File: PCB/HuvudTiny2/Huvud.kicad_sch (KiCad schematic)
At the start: 117 parts, among them J1 Conn_02x02_Odd_Even, J12 USB_Micro-B_Molex-105017-0001, J2 DBG, J3 THERM, J4 FAN0, J5 FAN1, J6 Heater, J7 Endstop, J9 STEPPER, Q1 AO3400A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

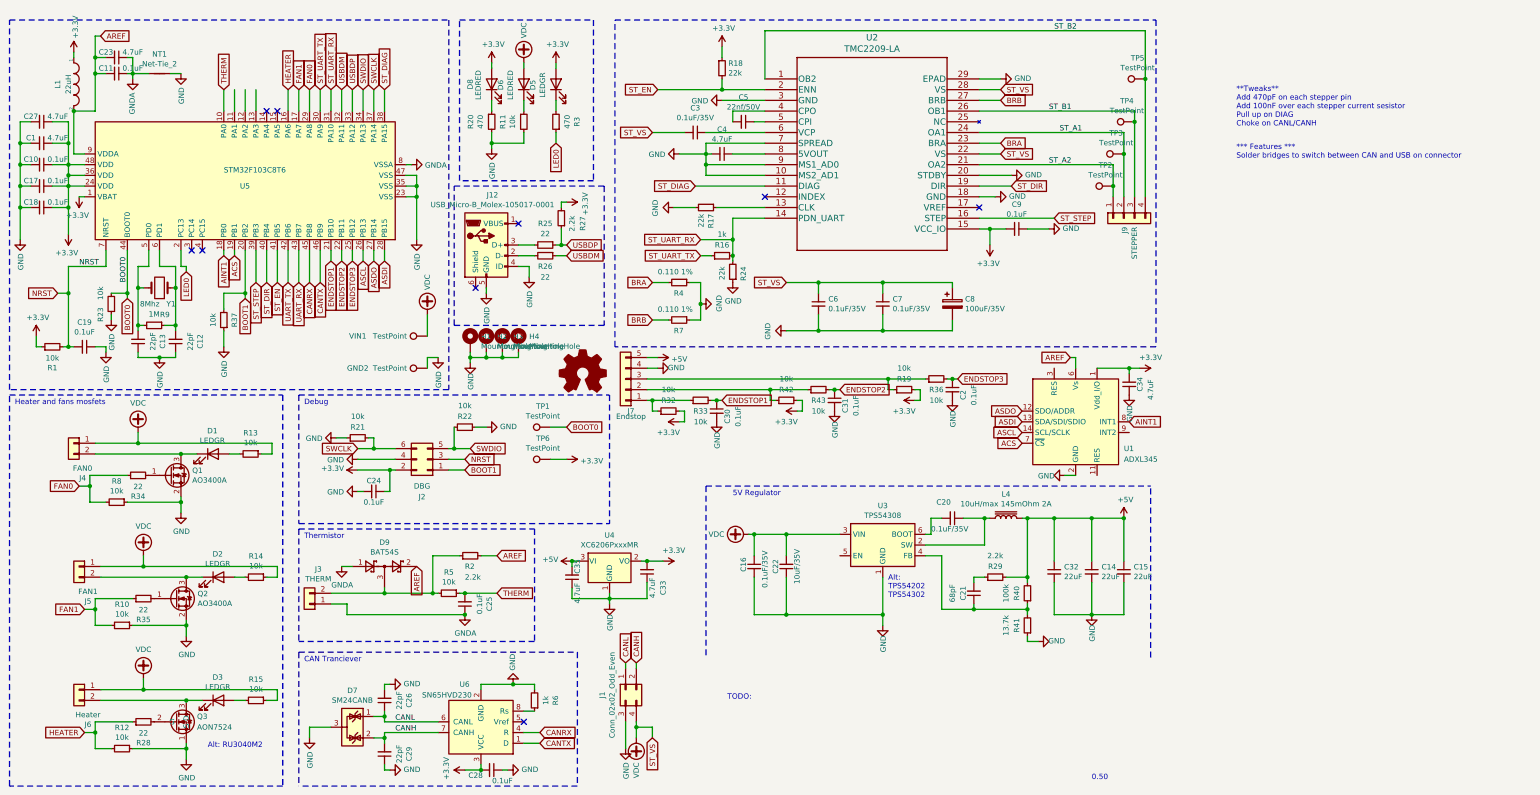
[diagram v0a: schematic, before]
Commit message: Power from USB, remove CAN. Update micro USB footprint. Update TMC footprint.
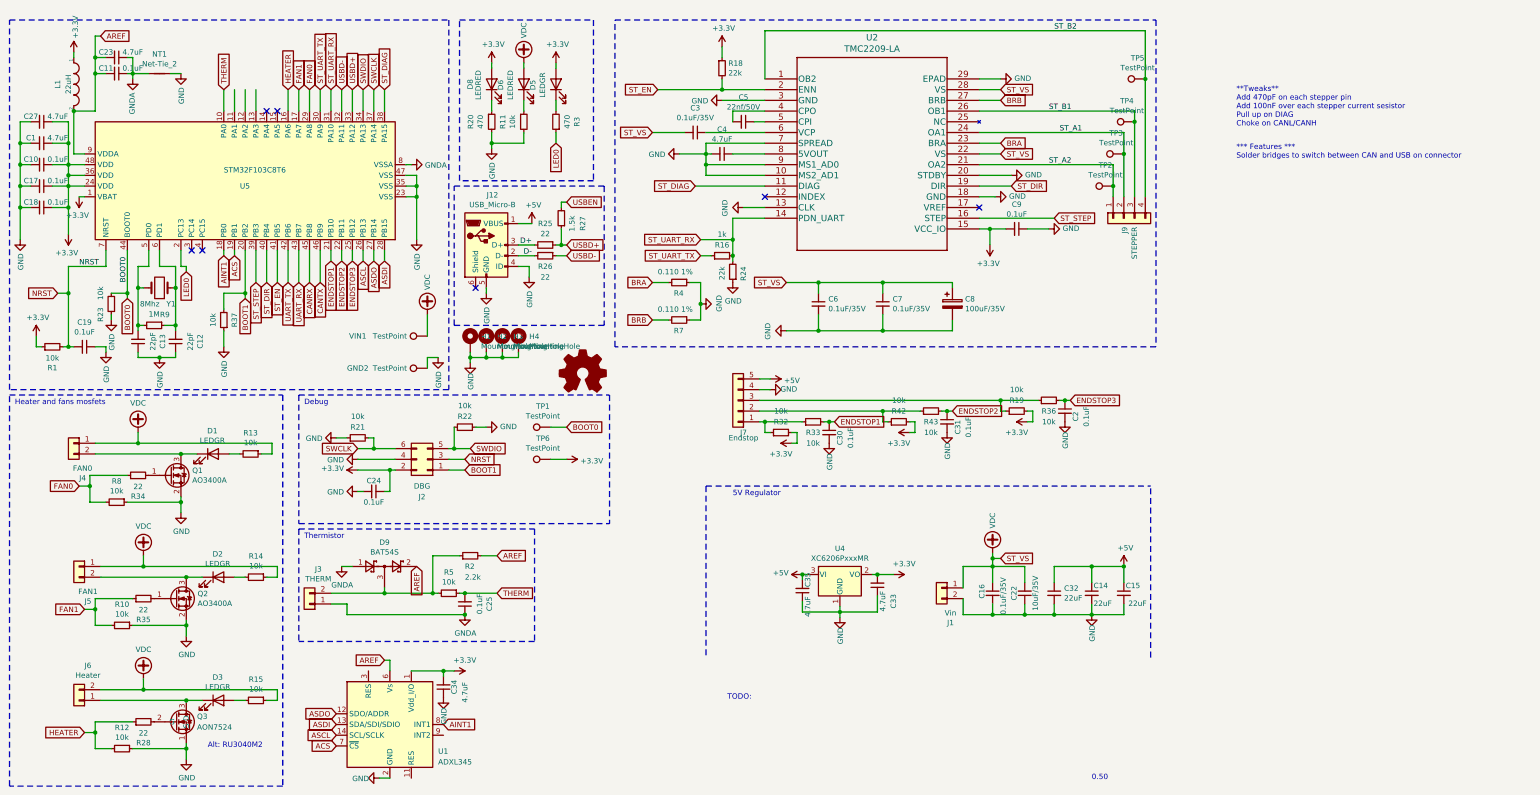
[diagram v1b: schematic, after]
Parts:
- removed C20: 0.1uF/35V, Capacitor_SMD:C_0603_1608Metric, symbol Device:C_Small
- removed C21: 68pF, Capacitor_SMD:C_0402_1005Metric, symbol Device:C_Small
- removed C26, C29: 22pF, Capacitor_SMD:C_0402_1005Metric, symbol Device:C_Small
- removed C28: 0.1uF, Capacitor_SMD:C_0402_1005Metric, symbol Device:C_Small
- removed D7: SM24CANB, Package_TO_SOT_SMD:SOT-23, symbol Power_Protection:NUP2105L
- removed J1: Conn_02x02_Odd_Even, Connector_Molex:Molex_Micro-Fit_3.0_43045-0400_2x02_P3.00mm_Horizontal, symbol Connector_Generic:Conn_02x02_Top_Bottom
- removed L4: 10uH/max 145mOhm 2A, Inductor_SMD:L_Sunlord_MWSA0518_5.4x5.2mm, symbol Device:L_Core_Iron
- removed R17: 22k, Resistor_SMD:R_0402_1005Metric, symbol Device:R_Small
- removed R29: 2.2k, Resistor_SMD:R_0402_1005Metric, symbol Device:R_Small
- removed R40: 100k, Resistor_SMD:R_0402_1005Metric, symbol Device:R_Small
- removed R41: 13.7k, Resistor_SMD:R_0402_1005Metric, symbol Device:R_Small
- removed R6: 1k, Resistor_SMD:R_0402_1005Metric, symbol Device:R_Small
- removed U3: TPS54308, Package_TO_SOT_SMD:SOT-23-6, symbol Regulator_Switching:TPS54308
- removed U6: SN65HVD230, Package_SO:SOIC-8_3.9x4.9mm_P1.27mm, symbol Interface_CAN_LIN:SN65HVD230
- added J1: Vin, Huvud:TerminalBlock_TE_282834-2_1x02_P2.54mm_Horizontal, symbol Connector_Generic:Conn_01x02
- J12: value USB_Micro-B_Molex-105017-0001 -> USB_Micro-B; footprint Connector_USB:USB_Micro-B_Molex-105017-0001 -> Huvud:MC-101C
- R27: value 2.2k -> 1.5k
- U2: footprint TMC2209:TMC2209-LA -> Huvud:TMC22xx_QFN
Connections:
- net +3V3: no longer R27.2
- net +5V: now also J12.1 (VBUS)
- net GND: now also U2.13 (CLK), J1.2 (Pin_2)
- net VDC: now also J6.2 (Pin_2), J1.1 (Pin_1); no longer J6.1 (Pin_1)
- net at D3.1 (K), Q3.3 (D): now also J6.1 (Pin_1); no longer J6.2 (Pin_2)
- net D-: now reaches J12.2 (D-), R26.2
- net D+: now reaches J12.3 (D+), R25.2
- net USBDM renamed USBD-
- net USBDP renamed USBD+
- new net USBEN: R27.2
- no-connect marks 9 -> 7
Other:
- note removed: "Alt: TPS54202 TPS54302"
- note removed: "CAN Tranciever"
- moved on the sheet: C14, C15, C16, C2, C22, C30, C31, C32, C33, C34, C35, J6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

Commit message: Improve power routing. Fix TH input protection.
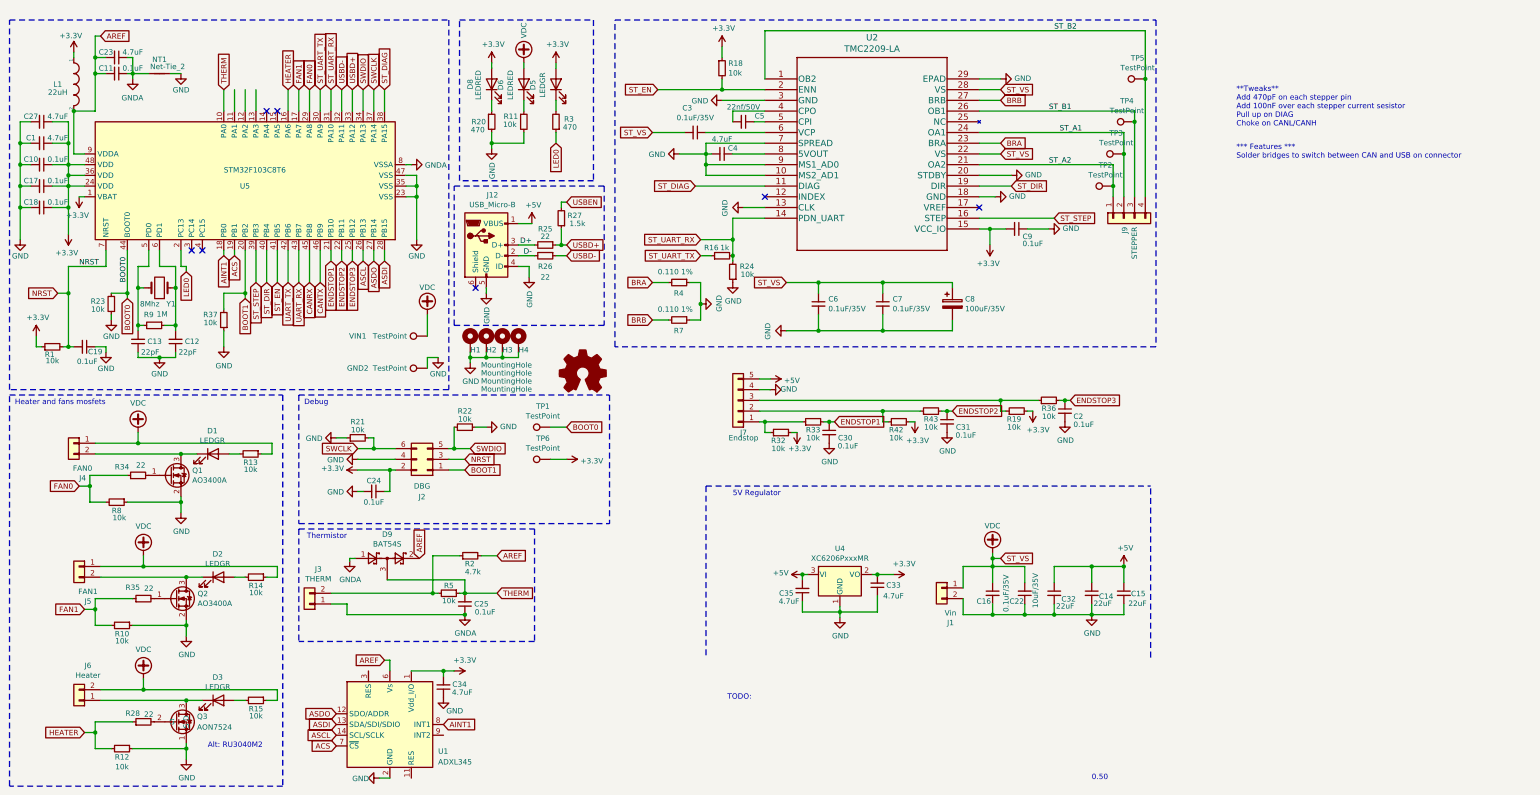
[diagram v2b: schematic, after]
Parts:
- R18, R24: value 22k -> 10k
- R2: value 2.2k -> 4.7k
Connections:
- net THERM: now also D9.3
- net at J3.2 (Pin_2), R2.1, R5.2: no longer D9.3
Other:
- moved on the sheet: D9

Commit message: Generated gerber files.
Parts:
- removed TP2, TP3, TP4, TP5: TestPoint, TestPoint:TestPoint_Pad_D1.0mm, symbol Connector:TestPoint
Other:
- note added: "**Tweaks** Add 470pF on each stepper pin Add 100nF over each stepper current sesistor"
- note removed: "*** Features *** Solder bridges to switch between CAN and USB on connector"
- note removed: "**Tweaks** Add 470pF on each stepper pin Add 100nF over each stepper current sesistor Pull up on DIAG Choke on CANL/CANH"
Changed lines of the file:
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@@
   (junction (at 269.24 143.51) (diameter 1.016) (color 0 0 0 0))
   (junction (at 269.24 154.94) (diameter 1.016) (color 0 0 0 0))
-  (junction (at 274.32 53.34) (diameter 1.016) (color 0 0 0 0))
-  (junction (at 276.86 45.72) (diameter 1.016) (color 0 0 0 0))
   (junction (at 276.86 143.51) (diameter 1.016) (color 0 0 0 0))
-  (junction (at 279.4 38.1) (diameter 1.016) (color 0 0 0 0))
-  (junction (at 281.94 27.94) (diameter 1.016) (color 0 0 0 0))
   (no_connect (at 55.88 68.58))
   (no_connect (at 58.42 68.58))
@@
     (stroke (width 0) (type solid) (color 0 0 0 0))
   )
-  (wire (pts (xy 274.32 48.26) (xy 274.32 53.34))
+  (wire (pts (xy 274.32 48.26) (xy 274.32 55.88))
     (stroke (width 0) (type solid) (color 0 0 0 0))
   )
-  (wire (pts (xy 274.32 53.34) (xy 274.32 55.88))
-    (stroke (width 0) (type solid) (color 0 0 0 0))
-  )
-  (wire (pts (xy 276.86 40.64) (xy 276.86 45.72))
-    (stroke (width 0) (type solid) (color 0 0 0 0))
-  )
-  (wire (pts (xy 276.86 45.72) (xy 276.86 55.88))
+  (wire (pts (xy 276.86 40.64) (xy 276.86 55.88))
     (stroke (width 0) (type solid) (color 0 0 0 0))
   )
@@
     (stroke (width 0) (type solid) (color 0 0 0 0))
   )
-  (wire (pts (xy 279.4 35.56) (xy 279.4 38.1))
-    (stroke (width 0) (type solid) (color 0 0 0 0))
-  )
-  (wire (pts (xy 279.4 38.1) (xy 279.4 55.88))
+  (wire (pts (xy 279.4 35.56) (xy 279.4 55.88))
     (stroke (width 0) (type solid) (color 0 0 0 0))
   )
-  (wire (pts (xy 281.94 16.51) (xy 281.94 27.94))
-    (stroke (width 0) (type solid) (color 0 0 0 0))
-  )
-  (wire (pts (xy 281.94 27.94) (xy 281.94 55.88))
+  (wire (pts (xy 281.94 16.51) (xy 281.94 55.88))
     (stroke (width 0) (type solid) (color 0 0 0 0))
   )
@@
     (effects (font (size 1.27 1.27)) (justify left bottom))
   )
-  (text "**Tweaks**\nAdd 470pF on each stepper pin\nAdd 100nF over each stepper current sesistor\nPull up on DIAG\nChoke on CANL/CANH\n"
+  (text "**Tweaks**\nAdd 470pF on each stepper pin\nAdd 100nF over each stepper current sesistor"
     (at 303.53 39.37 0)
     (effects (font (size 1.27 1.27)) (justify left bottom))
   )
-  (text "*** Features ***\nSolder bridges to switch between CAN and USB on connector"
-    (at 303.53 46.99 0)
-    (effects (font (size 1.27 1.27)) (justify left bottom))
-  )
   (label "NRST" (at 29.21 72.39 0)
     (effects (font (size 1.27 1.27)) (justify left bottom))
@@
     (pin "1")
   )
-  (symbol (lib_id "Connector:TestPoint") (at 274.32 53.34 90) (unit 1)
-    (in_bom yes) (on_board yes)
-    (property "Reference" "TP2" (id 0) (at 272.4912 48.387 90))
-    (property "Value" "TestPoint" (id 1) (at 272.4912 50.6984 90))
-    (property "Footprint" "TestPoint:TestPoint_Pad_D1.0mm" (id 2) (at 274.32 48.26 0)
-      (effects (font (size 1.27 1.27)) hide)
-    )
-    (property "Datasheet" "~" (id 3) (at 274.32 48.26 0)
-      (effects (font (size 1.27 1.27)) hide)
-    )
-    (pin "1")
-  )
-  (symbol (lib_id "Connector:TestPoint") (at 276.86 45.72 90) (unit 1)
-    (in_bom yes) (on_board yes)
-    (property "Reference" "TP3" (id 0) (at 275.0312 40.767 90))
-    (property "Value" "TestPoint" (id 1) (at 275.0312 43.0784 90))
-    (property "Footprint" "TestPoint:TestPoint_Pad_D1.0mm" (id 2) (at 276.86 40.64 0)
-      (effects (font (size 1.27 1.27)) hide)
-    )
-    (property "Datasheet" "~" (id 3) (at 276.86 40.64 0)
-      (effects (font (size 1.27 1.27)) hide)
-    )
-    (pin "1")
-  )
-  (symbol (lib_id "Connector:TestPoint") (at 279.4 38.1 90) (unit 1)
-    (in_bom yes) (on_board yes)
-    (property "Reference" "TP4" (id 0) (at 277.5712 33.147 90))
-    (property "Value" "TestPoint" (id 1) (at 277.5712 35.4584 90))
-    (property "Footprint" "TestPoint:TestPoint_Pad_D1.0mm" (id 2) (at 279.4 33.02 0)
-      (effects (font (size 1.27 1.27)) hide)
-    )
-    (property "Datasheet" "~" (id 3) (at 279.4 33.02 0)
-      (effects (font (size 1.27 1.27)) hide)
-    )
-    (pin "1")
-  )
-  (symbol (lib_id "Connector:TestPoint") (at 281.94 27.94 90) (unit 1)
-    (in_bom yes) (on_board yes)
-    (property "Reference" "TP5" (id 0) (at 280.1112 22.987 90))
-    (property "Value" "TestPoint" (id 1) (at 280.1112 25.2984 90))
-    (property "Footprint" "TestPoint:TestPoint_Pad_D1.0mm" (id 2) (at 281.94 22.86 0)
-      (effects (font (size 1.27 1.27)) hide)
-    )
-    (property "Datasheet" "~" (id 3) (at 281.94 22.86 0)
-      (effects (font (size 1.27 1.27)) hide)
-    )
-    (pin "1")
-  )
   (symbol (lib_id "power:GND") (at 15.24 66.04 0) (unit 1)
     (in_bom yes) (on_board yes)
@@
       (reference "TP1") (unit 1) (value "TestPoint") (footprint "TestPoint:TestPoint_Pad_D1.0mm")
     )
-    (path "/00000000-0000-0000-0000-00005f5636aa"
-      (reference "TP2") (unit 1) (value "TestPoint") (footprint "TestPoint:TestPoint_Pad_D1.0mm")
-    )
-    (path "/00000000-0000-0000-0000-00005f4cbb8b"
-      (reference "TP3") (unit 1) (value "TestPoint") (footprint "TestPoint:TestPoint_Pad_D1.0mm")
-    )
-    (path "/00000000-0000-0000-0000-00005f4a4be7"
-      (reference "TP4") (unit 1) (value "TestPoint") (footprint "TestPoint:TestPoint_Pad_D1.0mm")
-    )
-    (path "/00000000-0000-0000-0000-00005f4a34d5"
-      (reference "TP5") (unit 1) (value "TestPoint") (footprint "TestPoint:TestPoint_Pad_D1.0mm")
-    )
     (path "/00000000-0000-0000-0000-00005f623ed1"

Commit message: Add all R1 files - sent to fab.
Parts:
- C11, C17, C18, C19, C2, C24, C25, C30, C31: LCSC (none) -> C1525
- C13: LCSC (none) -> C1555
- C8: footprint Capacitor_SMD:CP_Elec_6.3x5.8 -> Capacitor_SMD:CP_Elec_6.3x7.7; LCSC C249982 -> C134792
- D1, D2, D3, D5: LCSC C74338 -> C130723
- D9: LCSC C181201 -> C12765
- J12: LCSC C10418 -> C183609
- J2: LCSC (none) -> C402781
- J3, J4, J5: LCSC (none) -> C225188
- J7: LCSC (none) -> C225191
- J9: LCSC C132474 -> C492489
- Q3: LCSC C431195 -> C115844
- R11, R19, R22, R32, R33, R36, R37, R42, R43: LCSC (none) -> C25744
- R16: LCSC C21190 -> C11702
- R18, R24: LCSC C25768 -> C25744
- R2: LCSC C25879 -> C25900
- R26, R28, R35: LCSC (none) -> C25092
- R27: LCSC C25879 -> C25867
- R4, R7: footprint Resistor_SMD:R_1206_3216Metric -> Resistor_SMD:R_0805_2012Metric; LCSC C327071 -> C53899
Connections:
- net USBEN: now also U5.3 (PC14)
- no-connect marks 7 -> 6
